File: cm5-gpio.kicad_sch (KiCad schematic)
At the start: 7 parts

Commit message: neo m8m impl.
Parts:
- added TP16, TP17: TestPoint, TestPoint:TestPoint_Pad_D1.0mm, symbol Connector:TestPoint
- renumbered R2 to R1, R3 to R2, R1 to R3
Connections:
- net CAM_GPIO1 is gone; now on net GND: CM5-1.100 (CAM_GPIO1)
- net CAM_GPIO0: now also TP17.1
- net GND: now also TP16.1

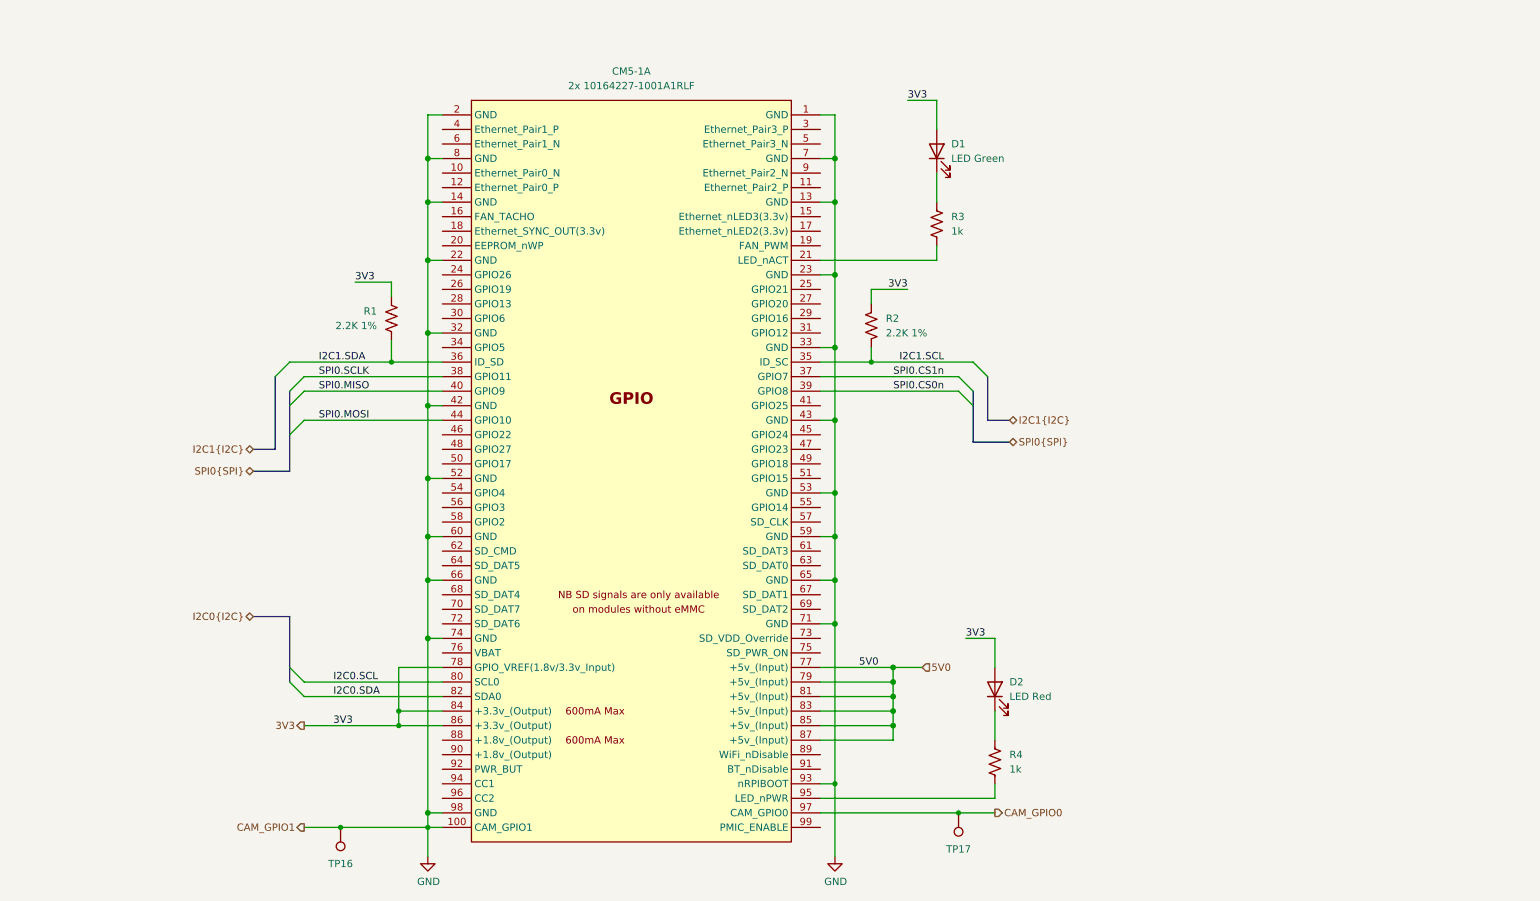
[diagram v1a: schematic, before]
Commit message: prepared usb3, abstracted cameras, backplane connector
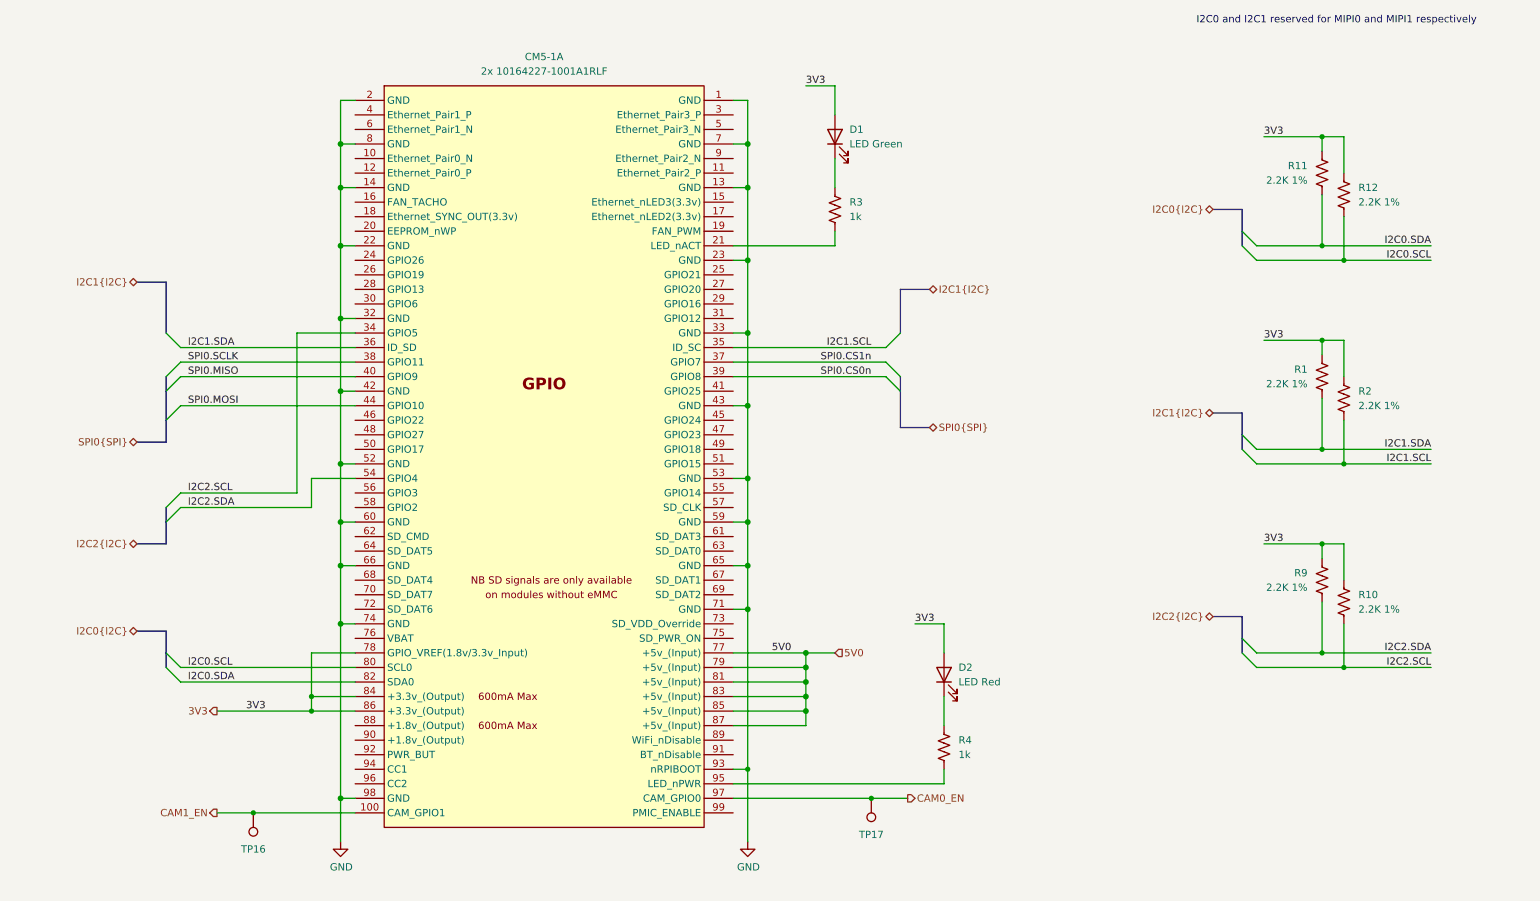
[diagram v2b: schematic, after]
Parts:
- added R10, R11, R12, R9: 2.2K 1%, Resistor_SMD:R_0402_1005Metric, symbol Device:R_US
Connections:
- net 3V3: now also R10.1, R11.1, R12.1, R9.1
- net GND: no longer CM5-1.100 (CAM_GPIO1), TP16.1
- net I2C0.SCL: now also R12.2
- net I2C0.SDA: now also R11.2
- net I2C2.SCL: now reaches CM5-1.34 (GPIO5)
- net I2C2.SCL: now also R10.2
- net I2C2.SDA: now reaches CM5-1.54 (GPIO4)
- net I2C2.SDA: now also R9.2
- net CAM_GPIO0 renamed CAM0_EN
- new net CAM1_EN: CM5-1.100 (CAM_GPIO1), TP16.1
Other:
- note added: "I2C0 and I2C1 reserved for MIPI0 and MIPI1 respectively"
- moved on the sheet: CM5-1A, D1, D2, R1, R3, R4, TP16, TP17

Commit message: moved power TPs to cm5 sheet
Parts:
- R1, R10, R11, R12, R2, R9: symbol Device:R_US -> library:R_US
- TP16, TP17: symbol Connector:TestPoint -> library:TestPoint
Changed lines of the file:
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@@
 	)
 	(symbol
-		(lib_id "Device:R_US")
+		(lib_id "library:R_US")
 		(at 252.73 77.47 0)
 		(unit 1)
@@
 	)
 	(symbol
-		(lib_id "Device:R_US")
+		(lib_id "library:R_US")
 		(at 256.54 116.84 0)
 		(unit 1)
@@
 	)
 	(symbol
-		(lib_id "Connector:TestPoint")
+		(lib_id "library:TestPoint")
 		(at 173.99 151.13 180)
 		(unit 1)
@@
 	)
 	(symbol
-		(lib_id "Device:R_US")
+		(lib_id "library:R_US")
 		(at 256.54 45.72 0)
 		(unit 1)
@@
 	)
 	(symbol
-		(lib_id "Device:R_US")
+		(lib_id "library:R_US")
 		(at 252.73 41.91 0)
 		(unit 1)
@@
 	)
 	(symbol
-		(lib_id "Device:R_US")
+		(lib_id "library:R_US")
 		(at 256.54 81.28 0)
 		(unit 1)
@@
 	)
 	(symbol
-		(lib_id "Connector:TestPoint")
+		(lib_id "library:TestPoint")
 		(at 66.04 153.67 180)
 		(unit 1)
@@
 	)
 	(symbol
-		(lib_id "Device:R_US")
+		(lib_id "library:R_US")
 		(at 252.73 113.03 0)
 		(unit 1)

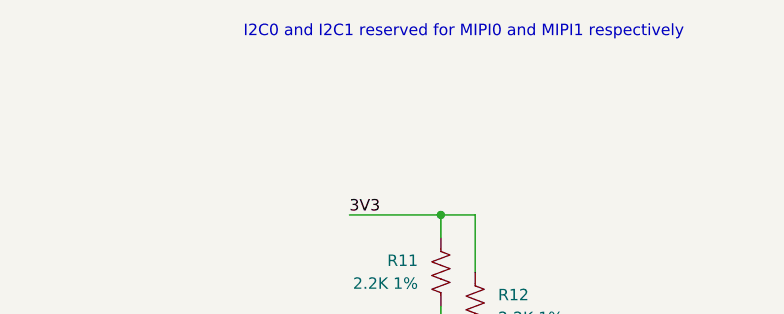
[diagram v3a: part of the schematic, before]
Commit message: added potential backplane conn
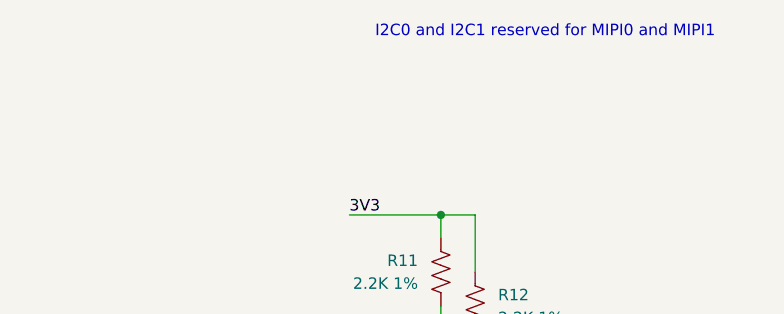
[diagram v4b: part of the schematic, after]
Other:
- note added: "I2C0 and I2C1 reserved for MIPI0 and MIPI1"
- note removed: "I2C0 and I2C1 reserved for MIPI0 and MIPI1 respectively"
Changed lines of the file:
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@@
 		(company "Andre S Winkel | Highlander Space Program | University of California, Riverside")
 	)
-	(text "I2C0 and I2C1 reserved for MIPI0 and MIPI1 respectively"
+	(text "I2C0 and I2C1 reserved for MIPI0 and MIPI1"
 		(exclude_from_sim no)
-		(at 255.27 15.24 0)
+		(at 283.21 15.24 0)
 		(effects
 			(font
 				(size 1.27 1.27)
 			)
+			(justify right)
 		)
 	)

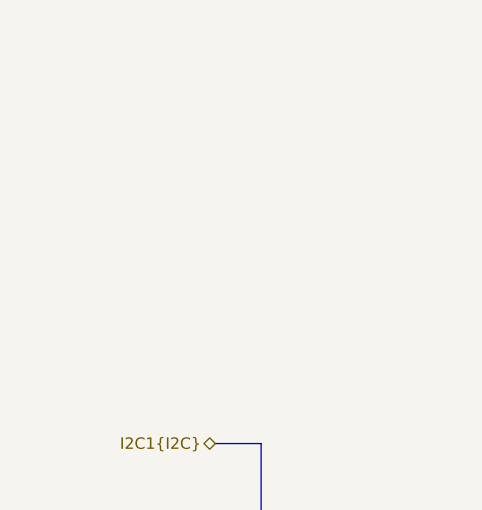
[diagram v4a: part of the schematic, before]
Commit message: added conns to backplane
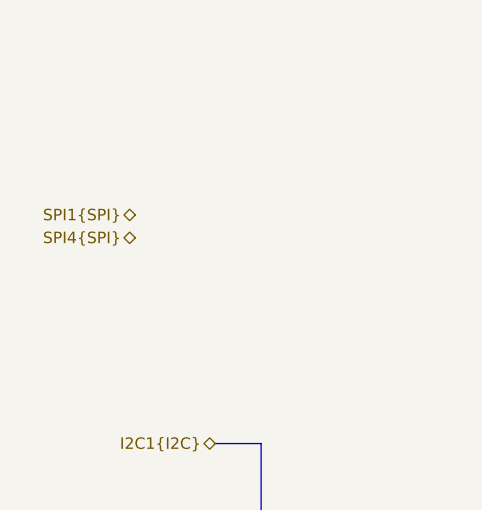
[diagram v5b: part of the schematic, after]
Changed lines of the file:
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@@
+		)
+	)
+	(hierarchical_label "SPI4{SPI}"
+		(shape bidirectional)
+		(at 36.83 38.1 180)
+		(effects
+			(font
+				(size 1.27 1.27)
+			)
+			(justify right)
 		)
 	)
@@
 		(effects
 			(font
+				(size 1.27 1.27)
+			)
+			(justify right)
+		)
+	)
+	(hierarchical_label "SPI1{SPI}"
+		(shape bidirectional)
+		(at 36.83 35.56 180)
+		(effects
+			(font

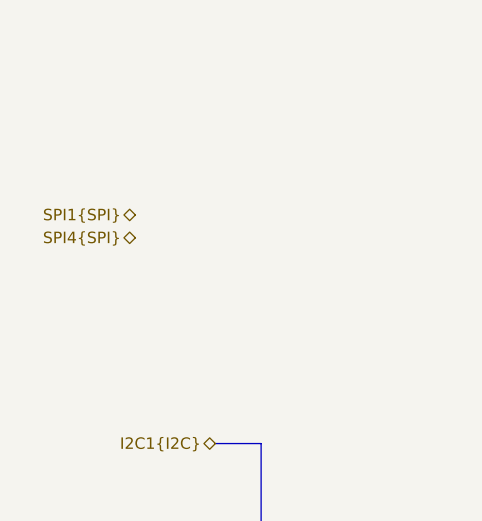
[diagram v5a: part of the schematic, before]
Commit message: removed ublox
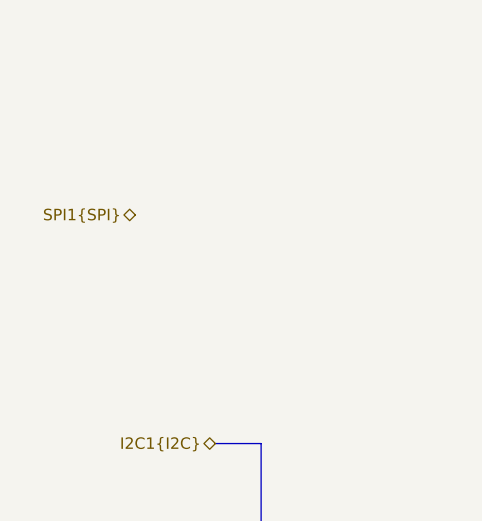
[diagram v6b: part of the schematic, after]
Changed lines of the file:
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@@
-		)
-	)
-	(hierarchical_label "SPI4{SPI}"
-		(shape bidirectional)
-		(at 36.83 38.1 180)
-		(effects
-			(font
-				(size 1.27 1.27)
-			)
-			(justify right)
 		)
 	)

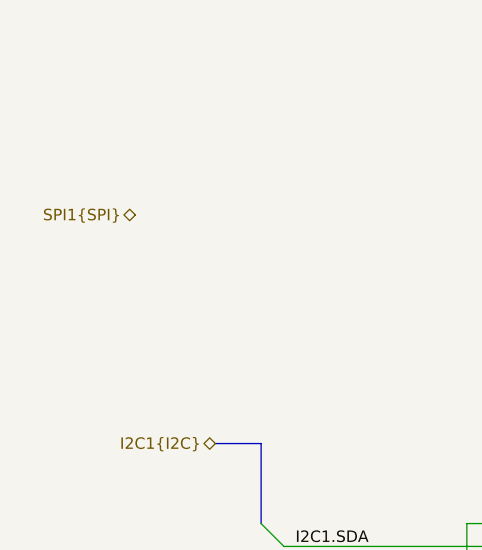
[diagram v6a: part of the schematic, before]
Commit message: defined can
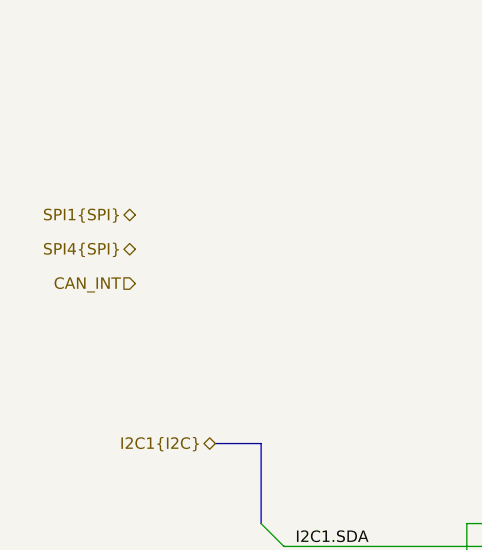
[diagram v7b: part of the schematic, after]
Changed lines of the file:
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@@
+		)
+	)
+	(hierarchical_label "CAN_INT"
+		(shape input)
+		(at 36.83 43.18 180)
+		(effects
+			(font
+				(size 1.27 1.27)
+			)
+			(justify right)
+		)
+	)
+	(hierarchical_label "SPI4{SPI}"
+		(shape bidirectional)
+		(at 36.83 39.37 180)
+		(effects
+			(font
+				(size 1.27 1.27)
+			)
+			(justify right)
 		)
 	)

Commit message: finished defining spi/i2c gpio, CAN, off-board signals
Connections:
- net SPI0.CS0n is gone; now on net I2C0.SDA: CM5-1.39 (GPIO8)
- net SPI0.MISO is gone; now on net I2C0.SCL: CM5-1.40 (GPIO9)
- net SPI0.MOSI is gone; now on net I2C1.SDA: CM5-1.44 (GPIO10)
- net SPI0.SCLK is gone; now on net I2C1.SCL: CM5-1.38 (GPIO11)
- net CAN_INT: now also CM5-1.41 (GPIO25)
- net I2C0.SCL: no longer CM5-1.80 (SCL0)
- net I2C0.SDA: no longer CM5-1.82 (SDA0)
- net I2C1.SCL: no longer CM5-1.35 (ID_SC)
- net I2C1.SDA: no longer CM5-1.36 (ID_SD)
- net I2C2.SCL: no longer CM5-1.34 (GPIO5)
- net I2C2.SDA: now also CM5-1.28 (GPIO13), CM5-1.31 (GPIO12); no longer CM5-1.54 (GPIO4)
- net SPI1.SCLK: now reaches CM5-1.25 (GPIO21)
- net SPI1.MISO: now reaches CM5-1.26 (GPIO19)
- net SPI1.MOSI: now reaches CM5-1.27 (GPIO20)
- net SPI3.MOSI: now reaches CM5-1.30 (GPIO6)
- net SPI1.CS0n: now reaches CM5-1.49 (GPIO18)
- net SPI1.CS1n: now reaches CM5-1.50 (GPIO17)
- net SPI2.SCLK: now reaches CM5-1.56 (GPIO3)
- net SPI2.MOSI: now reaches CM5-1.58 (GPIO2)
- net SPI0.CS1n renamed SPI3.SCLK
- new net SPI2.CS0n: CM5-1.36 (GPIO0)
- new net SPI2.MISO: CM5-1.35 (GPIO1)
- new net SPI3.CS0n: CM5-1.54 (GPIO4)
- new net SPI3.MISO: CM5-1.34 (GPIO5)
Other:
- moved on the sheet: R1, R10, R11, R12, R2, R9
